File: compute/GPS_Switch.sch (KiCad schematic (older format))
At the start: 0 parts

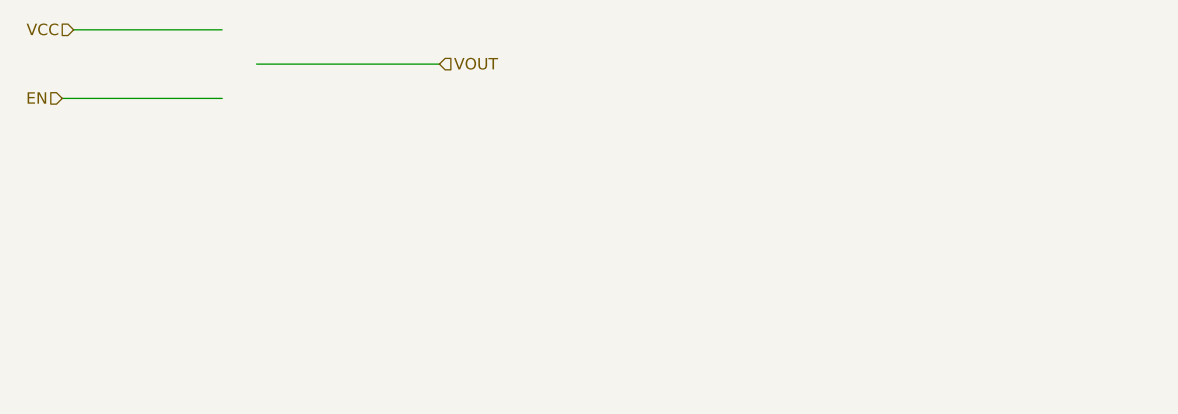
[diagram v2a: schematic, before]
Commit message: Adding Power Subsystem connector
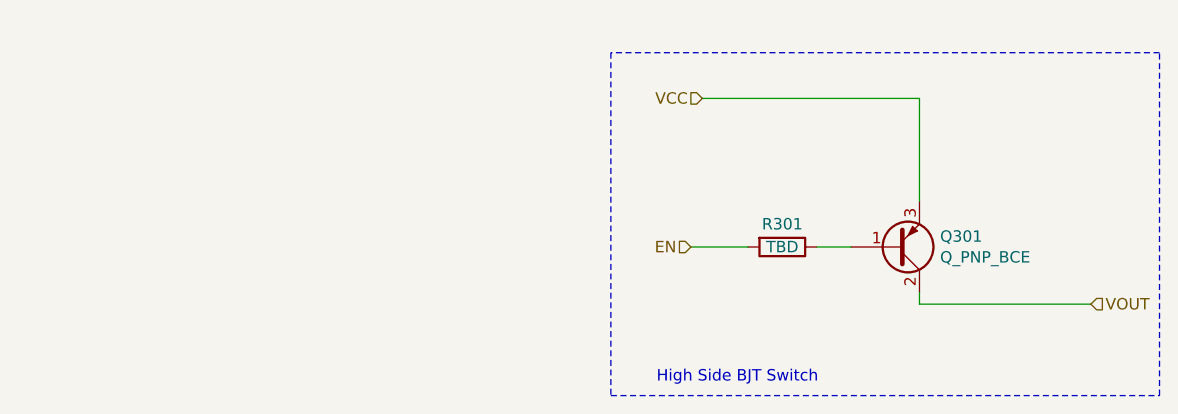
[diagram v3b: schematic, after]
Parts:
- added Q301: Q_PNP_BCE, symbol Device:Q_PNP_BCE
- added R301: TBD, symbol Device:R
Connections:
- wire segments 3 -> 6
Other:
- note added: "High Side BJT Switch"
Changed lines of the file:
@@
 Comment4 ""
 $EndDescr
-Wire Wire Line
-	2650 3200 3300 3200
-Text HLabel 2650 3200 0    50   Input ~ 0
+Text HLabel 5400 3500 0    50   Input ~ 0
 VCC
 Wire Wire Line
-	2600 3500 3300 3500
-Text HLabel 2600 3500 0    50   Input ~ 0
+	5350 4150 5600 4150
+Text HLabel 5350 4150 0    50   Input ~ 0
 EN
+Text HLabel 7100 4400 2    50   Input ~ 0
+VOUT
+$Comp
+L Device:Q_PNP_BCE Q301
+U 1 1 61C517AB
+P 6250 4150
+F 0 "Q301" H 6440 4104 50  0000 L CNN
+F 1 "Q_PNP_BCE" H 6440 4195 50  0000 L CNN
+F 2 "" H 6450 4250 50  0001 C CNN
+F 3 "~" H 6250 4150 50  0001 C CNN
+	1    6250 4150
+	1    0    0    1
+$EndComp
+$Comp
+L Device:R R301
+U 1 1 61C56989
+P 5750 4150
+F 0 "R301" V 5650 4150 50  0000 C CNN
+F 1 "TBD" V 5750 4150 50  0000 C CNN
+F 2 "" V 5680 4150 50  0001 C CNN
+F 3 "~" H 5750 4150 50  0001 C CNN
+	1    5750 4150
+	0    1    1    0
+$EndComp
 Wire Wire Line
-	3450 3350 4250 3350
-Text HLabel 4250 3350 2    50   Input ~ 0
-VOUT
+	5900 4150 6050 4150
+Wire Wire Line
+	6350 3950 6350 3500
+Wire Wire Line
+	6350 3500 5400 3500
+Wire Wire Line
+	6350 4350 6350 4400
+Wire Wire Line
+	6350 4400 7100 4400
+Text Notes 5200 4750 0    50   ~ 0
+High Side BJT Switch
+Wire Notes Line
+	7400 4800 7400 3300
+Wire Notes Line
+	7400 3300 5000 3300
+Wire Notes Line
+	5000 3300 5000 4800
+Wire Notes Line
+	5000 4800 7400 4800
 $EndSCHEMATC

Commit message: test points, footprints fixes, and layout fixes
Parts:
- R301: footprint (none) -> Resistor_SMD:R_0402_1005Metric_Pad0.72x0.64mm_HandSolder
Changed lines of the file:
@@
 F 0 "R301" V 5650 4150 50  0000 C CNN
 F 1 "TBD" V 5750 4150 50  0000 C CNN
-F 2 "" V 5680 4150 50  0001 C CNN
+F 2 "Resistor_SMD:R_0402_1005Metric_Pad0.72x0.64mm_HandSolder" V 5680 4150 50  0001 C CNN
 F 3 "~" H 5750 4150 50  0001 C CNN
 	1    5750 4150

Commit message: fixes to power and compute
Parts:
- Q301: footprint (none) -> Perch:TCN75AVOA713
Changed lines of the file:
@@
 $Descr A4 11693 8268
 encoding utf-8
-Sheet 3 3
+Sheet 2 2
 Title ""
 Date ""
@@
 F 0 "Q301" H 6440 4104 50  0000 L CNN
 F 1 "Q_PNP_BCE" H 6440 4195 50  0000 L CNN
-F 2 "" H 6450 4250 50  0001 C CNN
+F 2 "Perch:TCN75AVOA713" H 6450 4250 50  0001 C CNN
 F 3 "~" H 6250 4150 50  0001 C CNN
 	1    6250 4150

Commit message: Updated BOM on compute subsystem
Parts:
- Q301: footprint Perch:TCN75AVOA713 -> Perch:PBSS4140DPN; Description (none) -> BJT Transistor Array; MFN (none) -> Nexperia USA Inc.; MFP (none) -> PBSS4140DPN,115; S1PL (none) -> https://www.digikey.com/en/products/detail/nexperia-usa-inc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; S1PN (none) -> 1727-3896; S2PL (none) -> https://www.mouser.com/ProductDetail/Nexperia/PBSS4140DPN11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; S2PN (none) -> 771-PBSS4140DPN-T/R
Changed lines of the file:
@@
 F 0 "Q301" H 6440 4104 50  0000 L CNN
 F 1 "Q_PNP_BCE" H 6440 4195 50  0000 L CNN
-F 2 "Perch:TCN75AVOA713" H 6450 4250 50  0001 C CNN
-F 3 "~" H 6250 4150 50  0001 C CNN
+F 2 "Perch:PBSS4140DPN" H 6450 4250 50  0001 C CNN
+F 3 "https://assets.nexperia.com/documents/data-sheet/PBSS4140DPN.pdf" H 6250 4150 50  0001 C CNN
+F 4 "BJT Transistor Array" H 6250 4150 50  0001 C CNN "Description"
+F 5 "Nexperia USA Inc." H 6250 4150 50  0001 C CNN "MFN"
+F 6 "PBSS4140DPN,115" H 6250 4150 50  0001 C CNN "MFP"
+F 7 "https://www.digikey.com/en/products/detail/nexperia-usa-inc/PBSS4140DPN-115/1156926?utm_adgroup=Semiconductor%20Modules&utm_source=google&utm_medium=cpc&utm_campaign=Dynamic%20Search_EN_Product&utm_term=&utm_content=Semiconductor%20Modules&gclid=CjwKCAiAz--OBhBIEiwAG1rIOnfNYCfMx2ITlSYg59RzW_gpFrWZweD7vvrD8bBxi6JVwMmspkeghBoC1dkQAvD_BwE" H 6250 4150 50  0001 C CNN "S1PL"
+F 8 "1727-3896" H 6250 4150 50  0001 C CNN "S1PN"
+F 9 "https://www.mouser.com/ProductDetail/Nexperia/PBSS4140DPN115?qs=LOCUfHb8d9uI%2F4H%2FLdNjCQ%3D%3D" H 6250 4150 50  0001 C CNN "S2PL"
+F 10 "771-PBSS4140DPN-T/R" H 6250 4150 50  0001 C CNN "S2PN"
 	1    6250 4150
 	1    0    0    1

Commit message: some more updates to compute BOM
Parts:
- R301: Description (none) -> 470 Resistor; MFN (none) -> Yageo; MFP (none) -> RC0402FR-07470RL; S1PL (none) -> https://www.digikey.com/en/products/detail/RC0402FR-07470RL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; S1PN (none) -> 311-470LR; S2PL (none) -> https://www.mouser.com/ProductDetail/YAGEO/RC0402FR-07470RL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; S2PN (none) -> 603-RC0402FR-07470RL
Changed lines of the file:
@@
 F 1 "TBD" V 5750 4150 50  0000 C CNN
 F 2 "Resistor_SMD:R_0402_1005Metric_Pad0.72x0.64mm_HandSolder" V 5680 4150 50  0001 C CNN
-F 3 "~" H 5750 4150 50  0001 C CNN
+F 3 "https://www.yageo.com/upload/media/product/productsearch/datasheet/rchip/PYu-RC_Group_51_RoHS_L_11.pdf" H 5750 4150 50  0001 C CNN
+F 4 "470 Resistor" H 5750 4150 50  0001 C CNN "Description"
+F 5 "Yageo" H 5750 4150 50  0001 C CNN "MFN"
+F 6 "RC0402FR-07470RL" H 5750 4150 50  0001 C CNN "MFP"
+F 7 "https://www.digikey.com/en/products/detail/RC0402FR-07470RL/311-470LRTR-ND/726619?WT.z_cid=ref_netcomponents_dkc_buynow&utm_source=netcomponents&utm_medium=aggregator&utm_campaign=buynow" H 5750 4150 50  0001 C CNN "S1PL"
+F 8 "311-470LR" H 5750 4150 50  0001 C CNN "S1PN"
+F 9 "https://www.mouser.com/ProductDetail/YAGEO/RC0402FR-07470RL?qs=dn7UOKrNBAlPAr3vO7H4cA==&utm_source=netcomponents&utm_medium=aggregator&utm_campaign=RC0402FR-07470RL&utm_content=YAGEO" H 5750 4150 50  0001 C CNN "S2PL"
+F 10 "603-RC0402FR-07470RL" H 5750 4150 50  0001 C CNN "S2PN"
 	1    5750 4150
 	0    1    1    0
